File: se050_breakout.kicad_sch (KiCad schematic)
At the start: 9 parts, among them J1 Conn_01x05_Pin

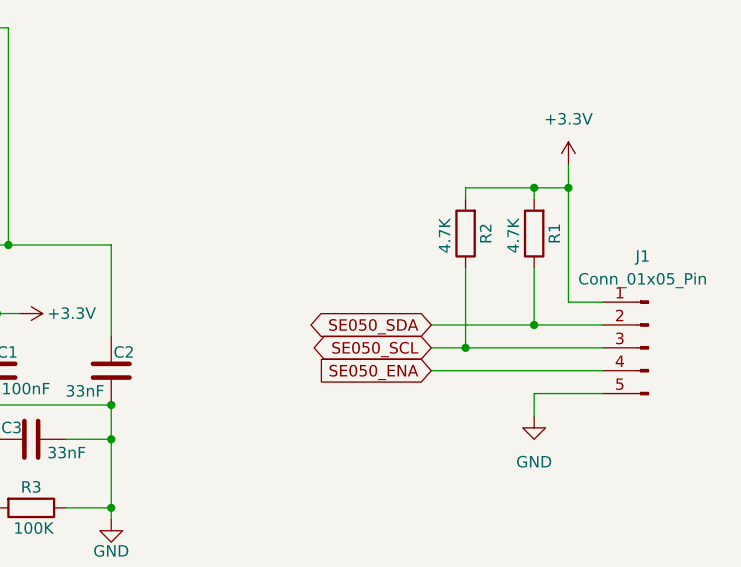
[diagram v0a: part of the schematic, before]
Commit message: Add JP1 solder jumper to tie ENA high without a spare GPIO
The SE050 comes up in deep power-down because R3 holds ENA low, so a
host that never drives that pin finds nothing at 0x48 - and firmware
commonly does ignore it, the Meshtastic SE050 driver among others.

JP1 is a bottom-side solder jumper between ENA and 3V3, shipped open:
bridge it and the part is permanently enabled, leave it open and drive
ENA from the header as before. Closing it costs only deep power-down
(<5 uA), the one mode that pad controls; software power-down with state
retention still works either way.

Gerbers regenerated from the updated board. The jumper lands on B.Cu,
B.Mask and B.Silkscreen but deliberately not on B.Paste - KiCad's solder
jumper footprints carry no paste aperture, so a stencil will not bridge
it by accident.

DRC on the updated board: 0 violations, 0 unconnected, 0 schematic
parity issues.
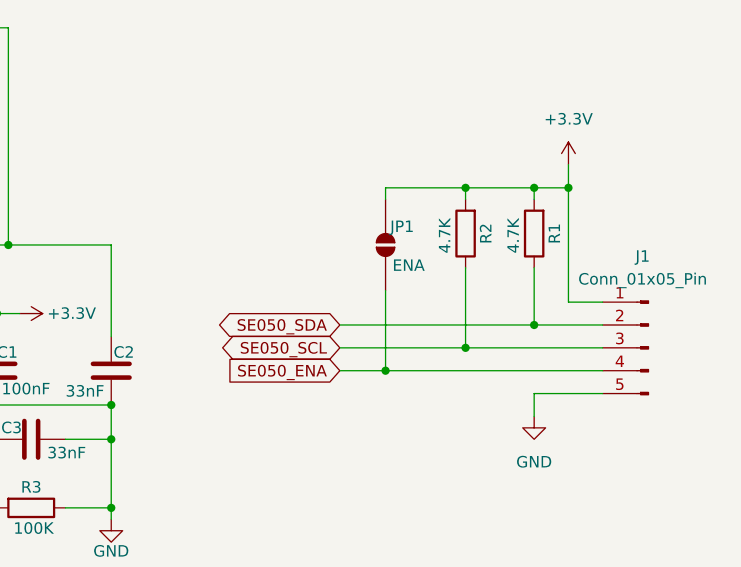
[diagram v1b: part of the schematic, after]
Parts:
- added JP1: ENA, Jumper:SolderJumper-2_P1.3mm_Open_RoundedPad1.0x1.5mm, symbol Jumper:SolderJumper_2_Open
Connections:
- net +3.3V: now also JP1.2 (B)
- net SE050_ENA: now also JP1.1 (A)
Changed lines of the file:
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@@
+	)
+	(junction
+		(at 118.11 115.57)
+		(diameter 0)
+		(color 0 0 0 0)
+	)
+	(junction
+		(at 135.89 115.57)
+		(diameter 0)
+		(color 0 0 0 0)
+	)
+	(junction
+		(at 135.89 107.95)
+		(diameter 0)
+		(color 0 0 0 0)
+	)
+	(junction
+		(at 80.01 59.69)
+		(diameter 0)
+		(color 0 0 0 0)
+	)
+	(junction
+		(at 175.26 97.79)
+		(diameter 0)
+		(color 0 0 0 0)
+	)
+	(junction
+		(at 92.71 59.69)
+		(diameter 0)
+		(color 0 0 0 0)
+	)
+	(junction
+		(at 166.37 100.33)
+		(diameter 0)
+		(color 0 0 0 0)
+	)
+	(junction
+		(at 175.26 80.01)
+		(diameter 0)
+		(color 0 0 0 0)
+	)
+	(junction
+		(at 182.88 80.01)
+		(diameter 0)
+		(color 0 0 0 0)
+	)
+	(junction
+		(at 186.69 80.01)
+		(diameter 0)
+		(color 0 0 0 0)
+	)
+	(junction
+		(at 124.46 86.36)
+		(diameter 0)
+		(color 0 0 0 0)
+	)
+	(junction
+		(at 118.11 107.95)
+		(diameter 0)
+		(color 0 0 0 0)
+	)
+	(junction
+		(at 135.89 104.14)
+		(diameter 0)
+		(color 0 0 0 0)
 	)
 	(junction
@@
 		(color 0 0 0 0)
 	)
-	(junction
-		(at 118.11 115.57)
-		(diameter 0)
-		(color 0 0 0 0)
-	)
-	(junction
-		(at 135.89 115.57)
-		(diameter 0)
-		(color 0 0 0 0)
-	)
-	(junction
-		(at 135.89 107.95)
-		(diameter 0)
-		(color 0 0 0 0)
-	)
-	(junction
-		(at 80.01 59.69)
-		(diameter 0)
-		(color 0 0 0 0)
-	)
-	(junction
-		(at 92.71 59.69)
-		(diameter 0)
-		(color 0 0 0 0)
-	)
-	(junction
-		(at 182.88 80.01)
-		(diameter 0)
-		(color 0 0 0 0)
-	)
-	(junction
-		(at 175.26 97.79)
-		(diameter 0)
-		(color 0 0 0 0)
-	)
-	(junction
-		(at 186.69 80.01)
-		(diameter 0)
-		(color 0 0 0 0)
-	)
-	(junction
-		(at 124.46 86.36)
-		(diameter 0)
-		(color 0 0 0 0)
-	)
-	(junction
-		(at 118.11 107.95)
-		(diameter 0)
-		(color 0 0 0 0)
-	)
-	(junction
-		(at 135.89 104.14)
-		(diameter 0)
-		(color 0 0 0 0)
-	)
 	(no_connect
 		(at 72.39 93.98)
@@
 	(wire
 		(pts
-			(xy 171.45 100.33) (xy 190.5 100.33)
+			(xy 161.29 100.33) (xy 166.37 100.33)
 		)
 		(stroke
@@
 	(wire
 		(pts
+			(xy 166.37 100.33) (xy 190.5 100.33)
+		)
+		(stroke
+			(width 0)
+			(type default)
+		)
+	)
+	(wire
+		(pts
 			(xy 95.25 62.23) (xy 95.25 64.77)
 		)
@@
 	(wire
 		(pts
-			(xy 171.45 95.25) (xy 182.88 95.25)
+			(xy 166.37 81.28) (xy 166.37 80.01)
+		)
+		(stroke
+			(width 0)
+			(type default)
+		)
+	)
+	(wire
+		(pts
+			(xy 161.29 95.25) (xy 182.88 95.25)
 		)
 		(stroke
@@
 	(wire
 		(pts
-			(xy 171.45 97.79) (xy 175.26 97.79)
+			(xy 161.29 97.79) (xy 175.26 97.79)
 		)
 		(stroke
@@
 	(wire
 		(pts
+			(xy 166.37 91.44) (xy 166.37 100.33)
+		)
+		(stroke
+			(width 0)
+			(type default)
+		)
+	)
+	(wire
+		(pts
 			(xy 186.69 77.47) (xy 186.69 80.01)
+		)
+		(stroke
+			(width 0)
+			(type default)
+		)
+	)
+	(wire
+		(pts
+			(xy 166.37 80.01) (xy 175.26 80.01)
 		)
 		(stroke
@@
 	(global_label "SE050_SCL"
 		(shape bidirectional)
-		(at 171.45 97.79 180)
+		(at 161.29 97.79 180)
 		(effects
 			(font
@@
 		)
 		(property "Intersheetrefs" "${INTERSHEET_REFS}"
-			(at 171.45 97.79 0)
+			(at 161.29 97.79 0)
 			(hide yes)
 			(show_name no)
@@
 	(global_label "SE050_SDA"
 		(shape bidirectional)
-		(at 171.45 95.25 180)
+		(at 161.29 95.25 180)
 		(effects
 			(font
@@
 		)
 		(property "Intersheetrefs" "${INTERSHEET_REFS}"
-			(at 171.45 95.25 0)
+			(at 161.29 95.25 0)
 			(hide yes)
 			(show_name no)
@@
 	(global_label "SE050_ENA"
 		(shape input)
-		(at 171.45 100.33 180)
+		(at 161.29 100.33 180)
 		(fields_autoplaced yes)
 		(effects
@@
 		)
 		(property "Intersheetrefs" "${INTERSHEET_REFS}"
-			(at 157.9421 100.33 0)
+			(at 147.7821 100.33 0)
 			(hide yes)
 			(show_name no)
@@
 					(unit 1)
 				)
+			)
+		)
+	)
+	(symbol
+		(lib_id "Jumper:SolderJumper_2_Open")
+		(at 166.37 86.36 90)
+		(unit 1)
+		(body_style 1)
+		(exclude_from_sim no)
+		(in_bom no)
+		(on_board yes)
+		(in_pos_files yes)
+		(dnp no)
+		(property "Reference" "JP1"
+			(at 166.878 84.328 90)
+			(show_name no)
+			(do_not_autoplace no)
+			(effects
+				(font
+					(size 1.27 1.27)
+				)
+				(justify right)
+			)
+		)
+		(property "Value" "ENA"
+			(at 167.132 88.646 90)
+			(show_name no)
+			(do_not_autoplace no)
+			(effects
+				(font
+					(size 1.27 1.27)
+				)
+				(justify right)
+			)
+		)
+		(property "Footprint" "Jumper:SolderJumper-2_P1.3mm_Open_RoundedPad1.0x1.5mm"
+			(at 166.37 86.36 0)
+			(hide yes)
+			(show_name no)
+			(do_not_autoplace no)
+			(effects
+				(font
+					(size 1.27 1.27)
+				)
+			)
+		)
+		(property "Datasheet" ""
+			(at 173.99 86.36 0)
+			(hide yes)
+			(show_name no)
+			(do_not_autoplace no)
+			(effects
+				(font
+					(size 1.27 1.27)
+				)
+			)
+		)
+		(property "Description" "Solder Jumper, 2-pole, open"
+			(at 171.45 86.36 0)
+			(hide yes)
+			(show_name no)
+			(do_not_autoplace no)
+			(effects
+				(font
+					(size 1.27 1.27)
+				)
+			)
+		)
+		(pin "1"
+		)
+		(pin "2"
+		)
+		(instances
+			(project "se050_breakout"
+				(path "/a418139e-e8a6-4ac5-b762-d44d34b12a0b"
+					(reference "JP1")
+					(unit 1)
+				)

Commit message: Tie SE050 RST_N to ground instead of the 3V3 rail
Pin 14 is referenced to VCC, and VCC reaches the die from VOUT through
an internal switch that opens in deep power-down. Since R3 holds ENA low
by default, deep power-down is this board's resting state: VCC sits at
0 V while VIN stays at 3.3 V, leaving a pin tied to the rail above its
own reference.

The data sheet allows either VCC or VSS for this pad, and VSS is the one
that holds in every state. It cannot hold the part in reset either,
because RST_N is only active when the ISO7816 interface is enabled,
which is not the case on generic E2 parts.

Gerbers regenerated. DRC: 0 violations, 0 unconnected, 0 schematic
parity issues.
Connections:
- net +3.3V: no longer SE050.14 (ISO_7816_RST_N)
- net GND: now also SE050.14 (ISO_7816_RST_N)
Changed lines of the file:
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@@
 		(color 0 0 0 0)
 	)
+	(junction
+		(at 97.79 59.69)
+		(diameter 0)
+		(color 0 0 0 0)
+	)
 	(no_connect
 		(at 72.39 93.98)
@@
 	(wire
 		(pts
+			(xy 120.65 59.69) (xy 97.79 59.69)
+		)
+		(stroke
+			(width 0)
+			(type default)
+		)
+	)
+	(wire
+		(pts
 			(xy 182.88 102.87) (xy 182.88 105.41)
 		)
@@
 	(wire
 		(pts
-			(xy 123.19 88.9) (xy 123.19 93.98)
-		)
-		(stroke
-			(width 0)
-			(type default)
-		)
-	)
-	(wire
-		(pts
 			(xy 182.88 95.25) (xy 190.5 95.25)
 		)
@@
 	(wire
 		(pts
+			(xy 120.65 88.9) (xy 120.65 59.69)
+		)
+		(stroke
+			(width 0)
+			(type default)
+		)
+	)
+	(wire
+		(pts
 			(xy 135.89 96.52) (xy 135.89 86.36)
 		)
@@
 	(wire
 		(pts
+			(xy 118.11 88.9) (xy 120.65 88.9)
+		)
+		(stroke
+			(width 0)
+			(type default)
+		)
+	)
+	(wire
+		(pts
 			(xy 190.5 102.87) (xy 182.88 102.87)
 		)
@@
 		)
 		(stroke
-			(width 0)
-			(type default)
-		)
-	)
-	(wire
-		(pts
-			(xy 118.11 88.9) (xy 123.19 88.9)
-		)
-		(stroke

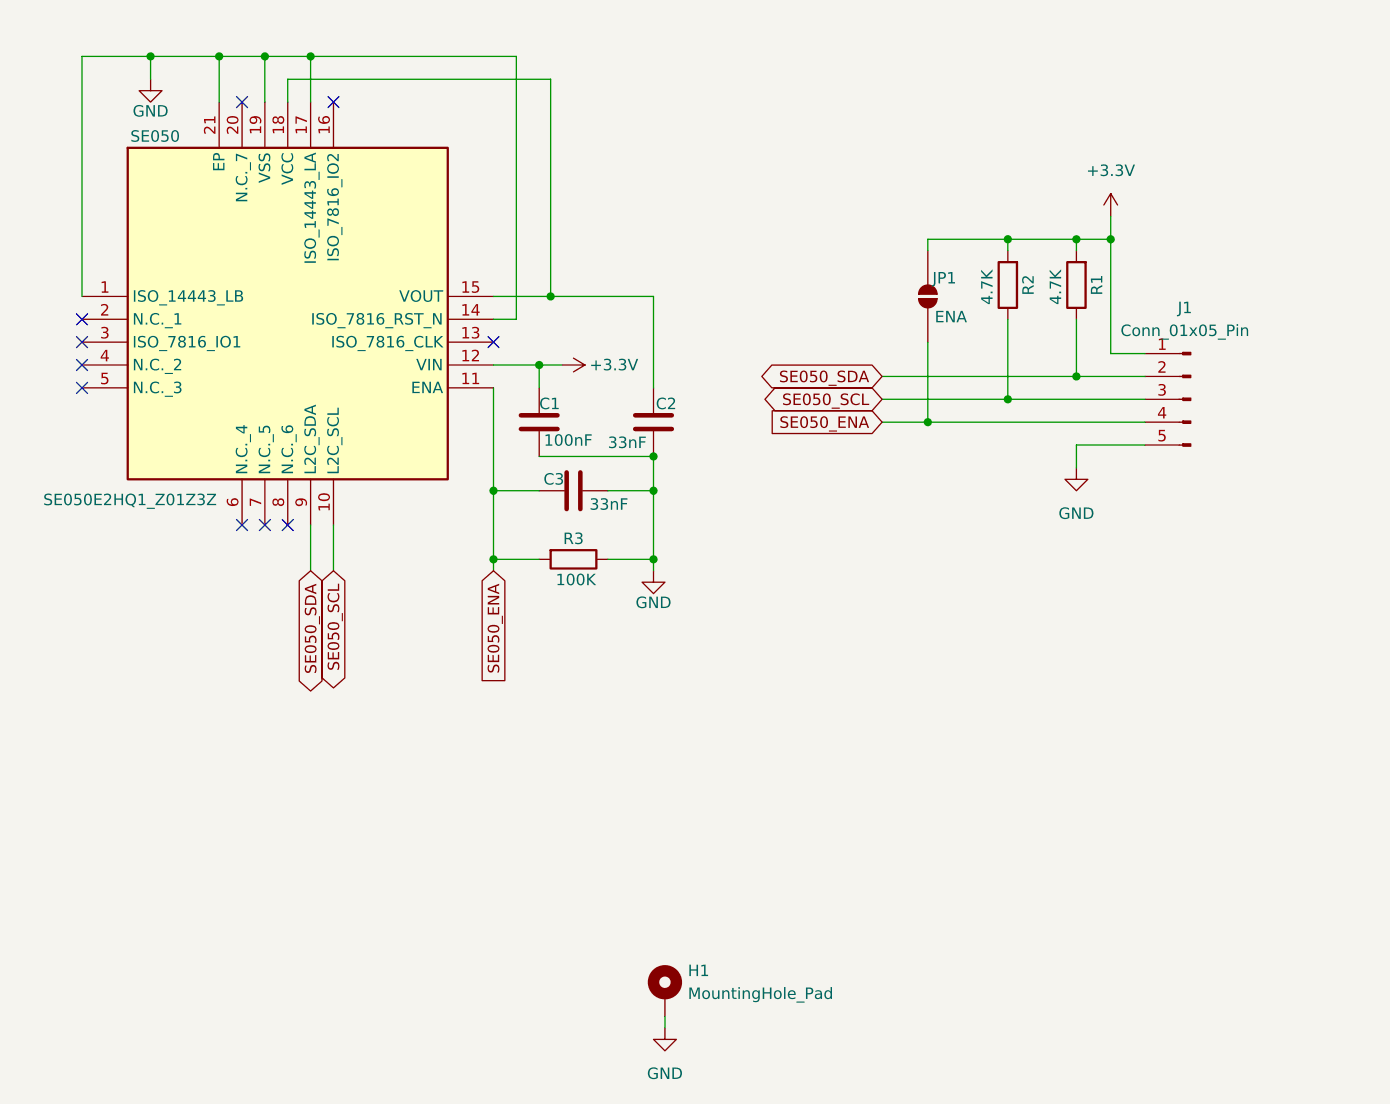
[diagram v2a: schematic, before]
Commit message: Add assembly fiducials and refresh the fabrication output
The board grows to 16.42 x 14.56 mm to make room for two 1 mm fiducials placed
diagonally, each with a 3 mm keepout drawn as a rule area on the top copper so
the ground pour backs away and leaves an assembly camera a clean target. The
circuit is unchanged; this only makes the board usable for machine assembly.

Correct the LCSC part number on R1 and R2. Both carried C60491, which is a
100k resistor, so a machine-assembled board would have shipped with 100k
pull-ups on the I2C bus instead of 4k7 and the SE050 would not have answered.

Regenerate gerber/. It still held the August layout and no longer matched the
board, so anyone ordering from it would have received the wrong outline.

Bring the README in line with the board: the bill of materials had a stale C2
and C3 from before the VOUT/VCC capacitor was removed, and it now carries the
LCSC numbers, the fiducial notes, and an accurate account of what has and has
not been fabricated.
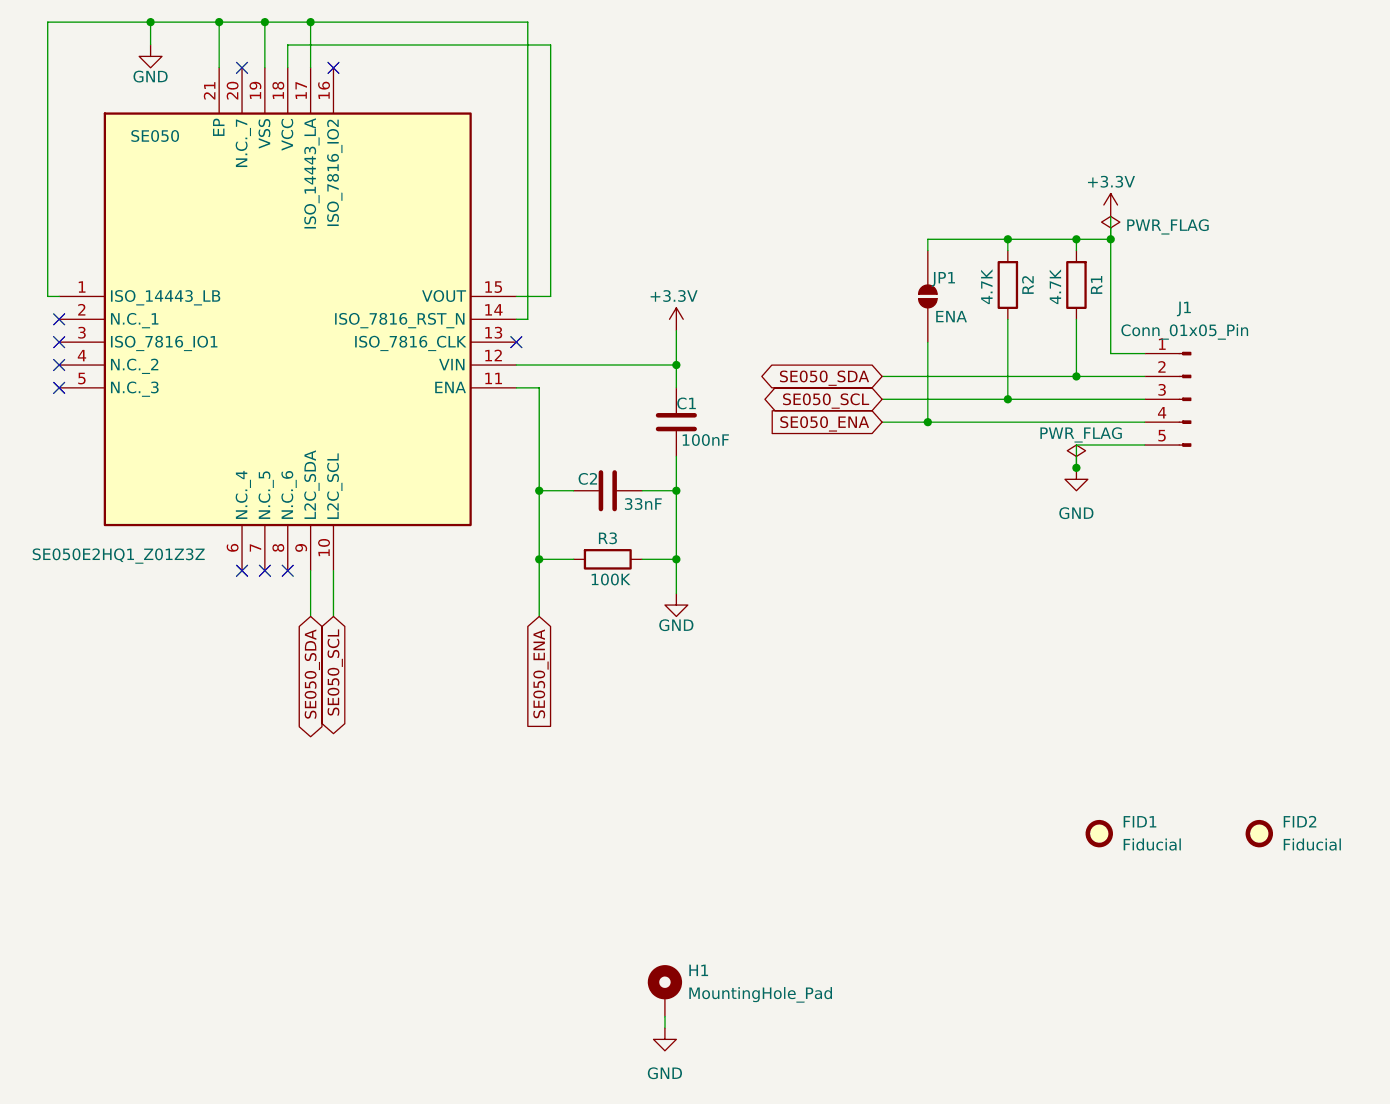
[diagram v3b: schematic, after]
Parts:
- removed C2: 33nF, Capacitor_SMD:C_0402_1005Metric, symbol Device:C
- added FID1, FID2: Fiducial, Fiducial:Fiducial_1mm_Mask2mm, symbol Mechanical:Fiducial
- J1: now left out of the parts list
- R1, R2: LCSC Part C60491 -> C105871
- SE050: Height (none) -> 0.33; Manufacturer_Name (none) -> NXP; Manufacturer_Part_Number (none) -> SE050E2HQ1/Z01Z3Z
- renumbered C3 to C2
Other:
- moved on the sheet: C1, C2, R3, SE050
